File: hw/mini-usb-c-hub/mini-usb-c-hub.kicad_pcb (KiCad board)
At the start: 4 copper layers, 0 parts

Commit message: chore(hw): choose usb-c receptacle
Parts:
- added J1: USB_C_Receptacle_USB2.0_16P, local:USB_C_Receptacle_G-Switch_GT-USB-7010ASV_shortened, F.Cu at (172.3, 102.8)
- added R1: 5k1, Resistor_SMD:R_0805_2012Metric_Pad1.20x1.40mm_HandSolder, F.Cu at (154.1, 100.2)
- added R2: 5k1, Resistor_SMD:R_0805_2012Metric_Pad1.20x1.40mm_HandSolder, F.Cu at (154.1, 103.2)
- added U101: FE1.1s, Package_SO:SSOP-28_3.9x9.9mm_P0.635mm, F.Cu at (134.0, 106.8)
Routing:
- net unconnected-(J1-SHIELD-PadS1): track 0.00 -> 17.0 mm
- net +5V: track 0.00 -> 7.76 mm, vias 0 -> 2
- net GND: track 0.00 -> 5.63 mm, vias 0 -> 1
- net unconnected-(J1-D--PadB7): track 0.00 -> 2.98 mm
- net Net-(J1-CC1): track 0.00 -> 2.97 mm
- net unconnected-(J1-SBU2-PadB8): track 0.00 -> 2.97 mm
- added copper zone on B.Cu, net GND
- added copper zone on F.Cu, net GND
- added copper zone on In1.Cu, net GND
- added copper zone on In2.Cu, net GND
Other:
- board outline added: 80 x 40 mm

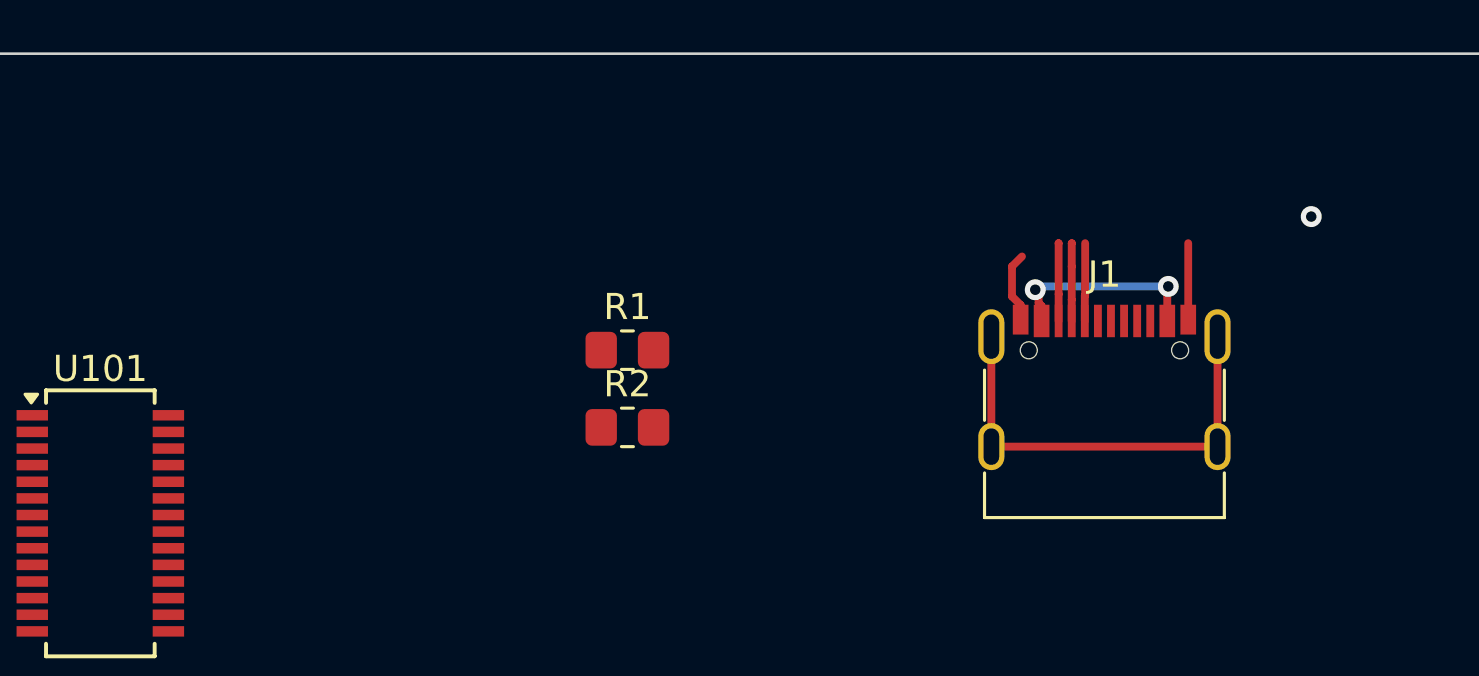
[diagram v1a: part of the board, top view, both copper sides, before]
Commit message: chore(hw): add data pins, move upstream connector
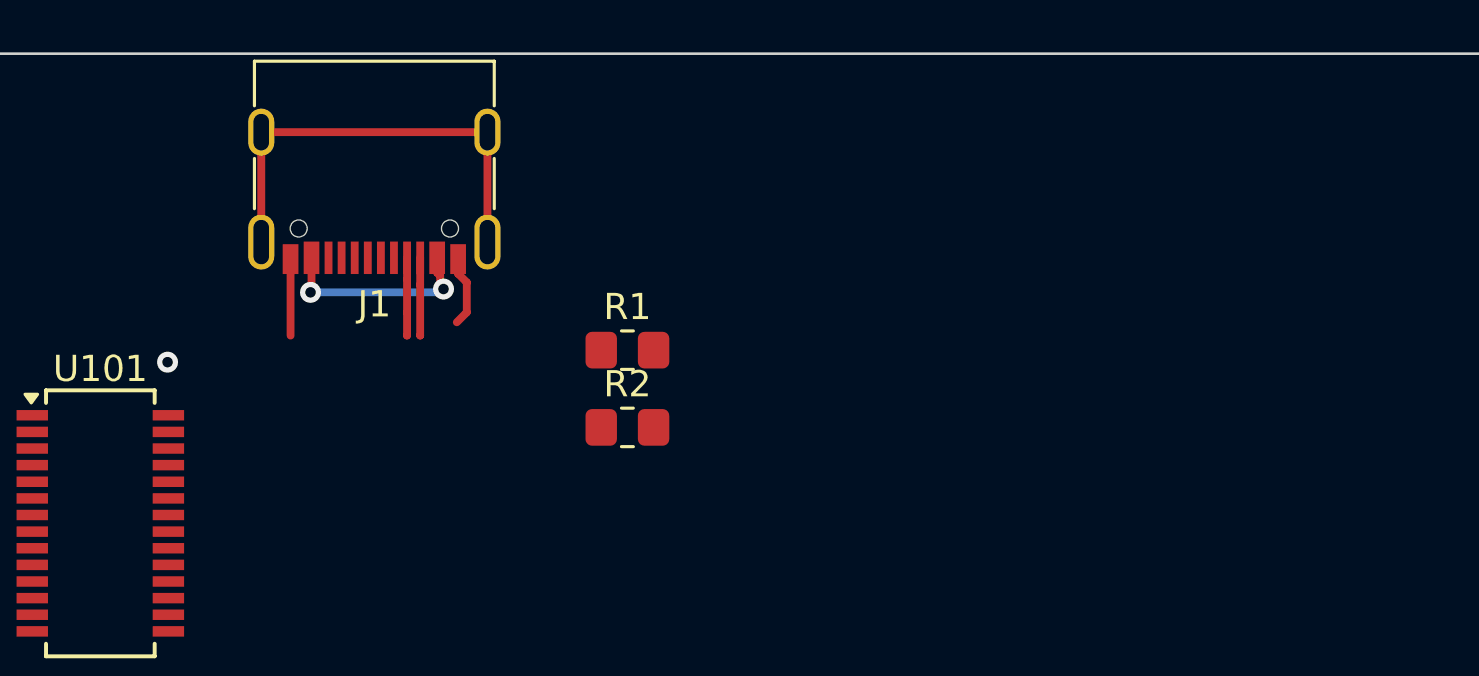
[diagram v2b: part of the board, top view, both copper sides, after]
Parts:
- moved J1 29.6 mm to (144.4, 93.0), turned to 180 degrees
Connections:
- J1 pad A6: unconnected-(J1-D+-PadA6) -> /Upstream Port/UD_P
- J1 pad A7: unconnected-(J1-D--PadA7) -> /Upstream Port/UD_N
- U101 pad 15: unconnected-(U101-DMU-Pad15) -> /Upstream Port/UD_N
- U101 pad 16: unconnected-(U101-DPU-Pad16) -> /Upstream Port/UD_P
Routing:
- net unconnected-(J1-D--PadB7): track 2.98 -> 0.00 mm

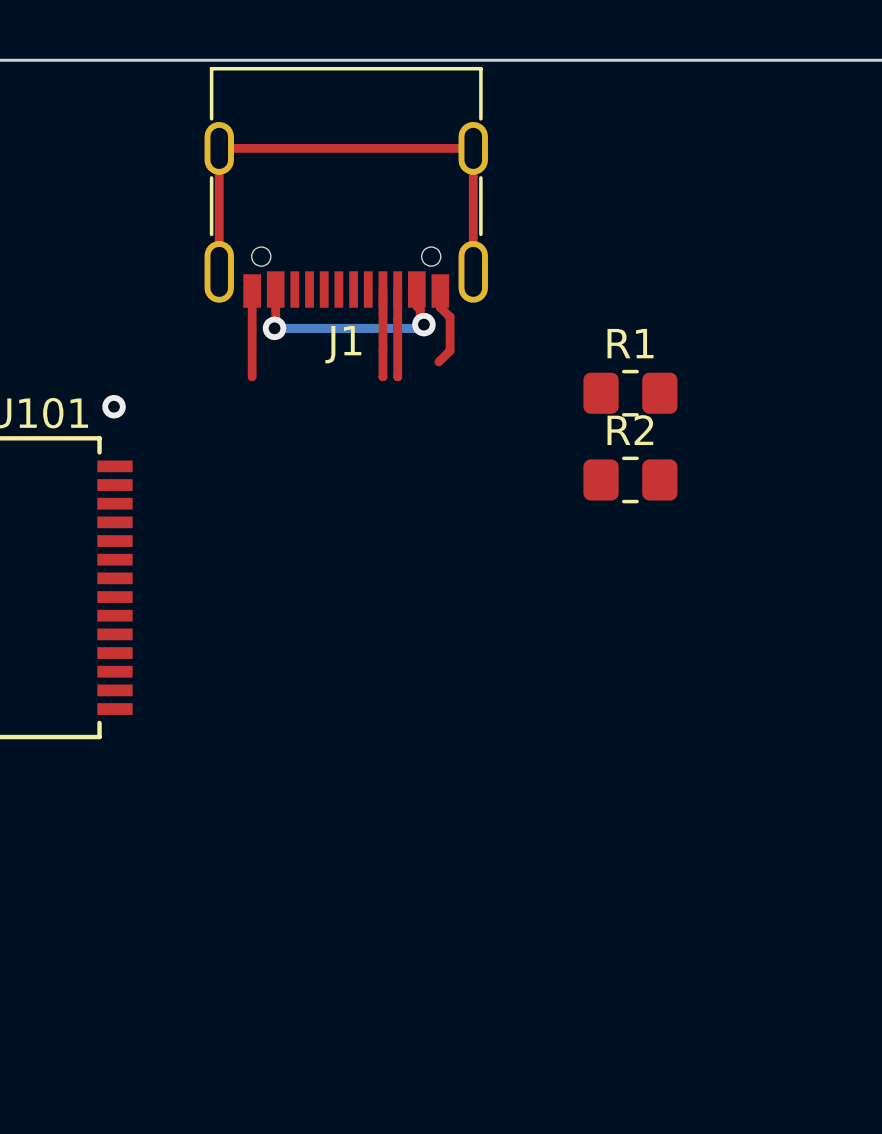
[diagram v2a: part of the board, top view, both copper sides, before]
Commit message: chore(hw): preliminary hub chip connections
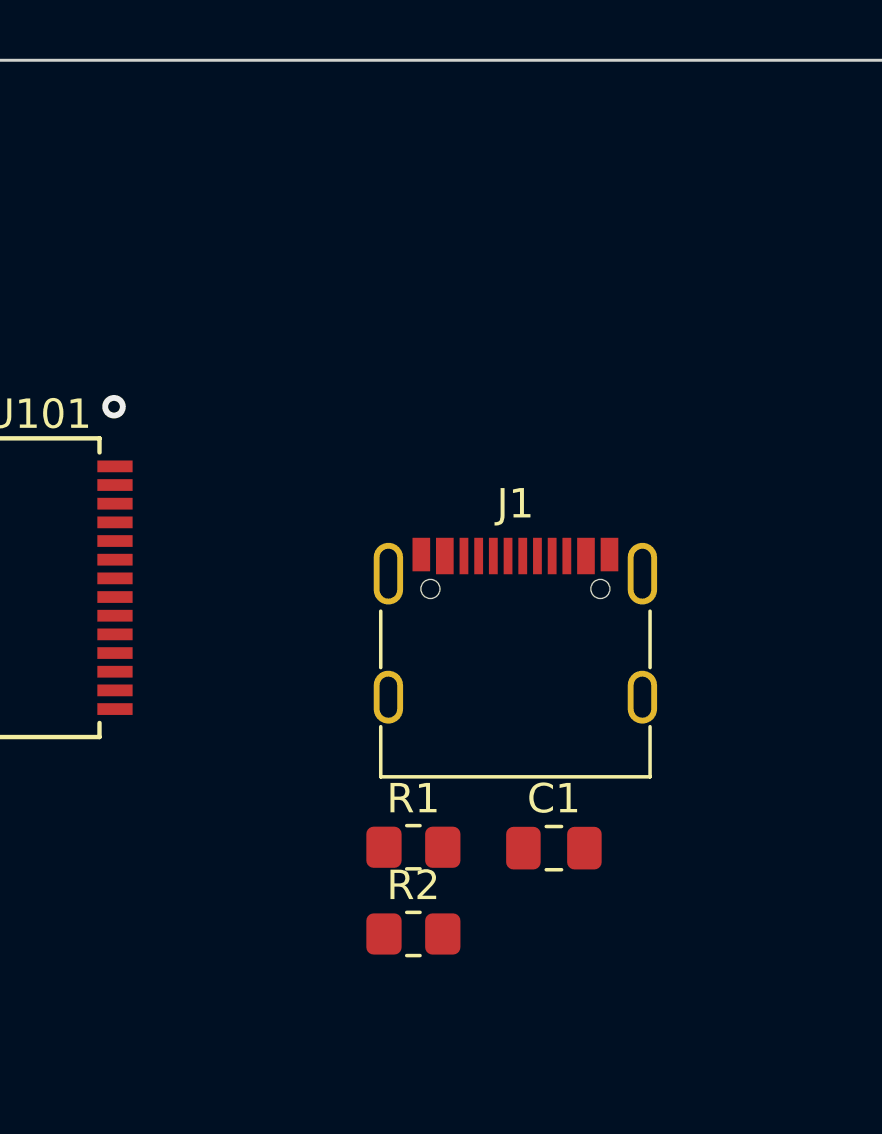
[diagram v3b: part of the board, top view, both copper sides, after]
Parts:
- added C1: C, Capacitor_SMD:C_0805_2012Metric_Pad1.18x1.45mm_HandSolder, F.Cu at (151.5, 115.7)
- moved J1 17.5 mm to (150.2, 109.5), turned to 0 degrees
- moved R1 17.1 mm to (146.7, 115.7)
- moved R2 17.1 mm to (146.7, 118.6)
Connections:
- net /Upstream Port/UD_N renamed /UD_N
- net /Upstream Port/UD_P renamed /UD_P
- J1 pad S1: unconnected-(J1-SHIELD-PadS1) -> Net-(J1-SHIELD)
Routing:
- net unconnected-(J1-SHIELD-PadS1): track 17.0 -> 0.00 mm
- net +5V: track 7.76 -> 0.00 mm, vias 2 -> 0
- net GND: track 5.63 -> 0.00 mm
- net Net-(J1-CC1): track 2.97 -> 0.00 mm
- net unconnected-(J1-SBU2-PadB8): track 2.97 -> 0.00 mm

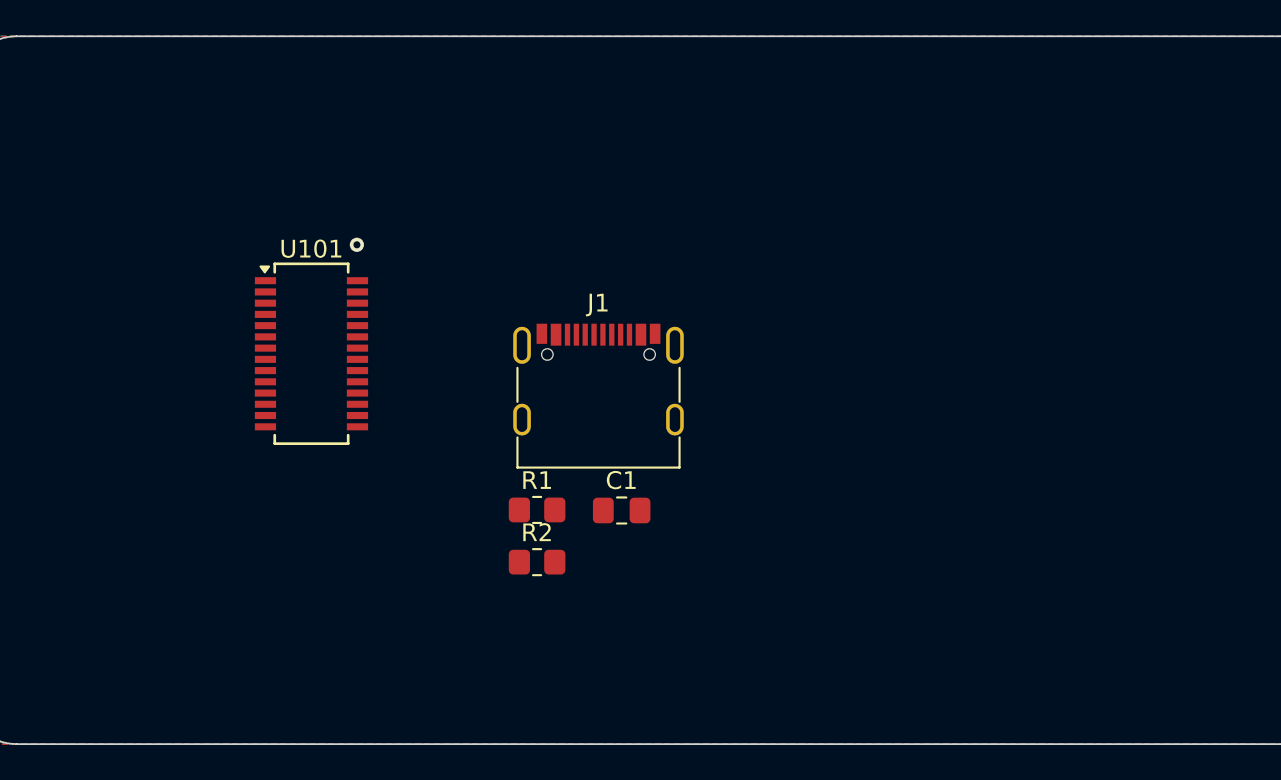
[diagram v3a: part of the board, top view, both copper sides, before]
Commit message: chore(hw): add downstream ports
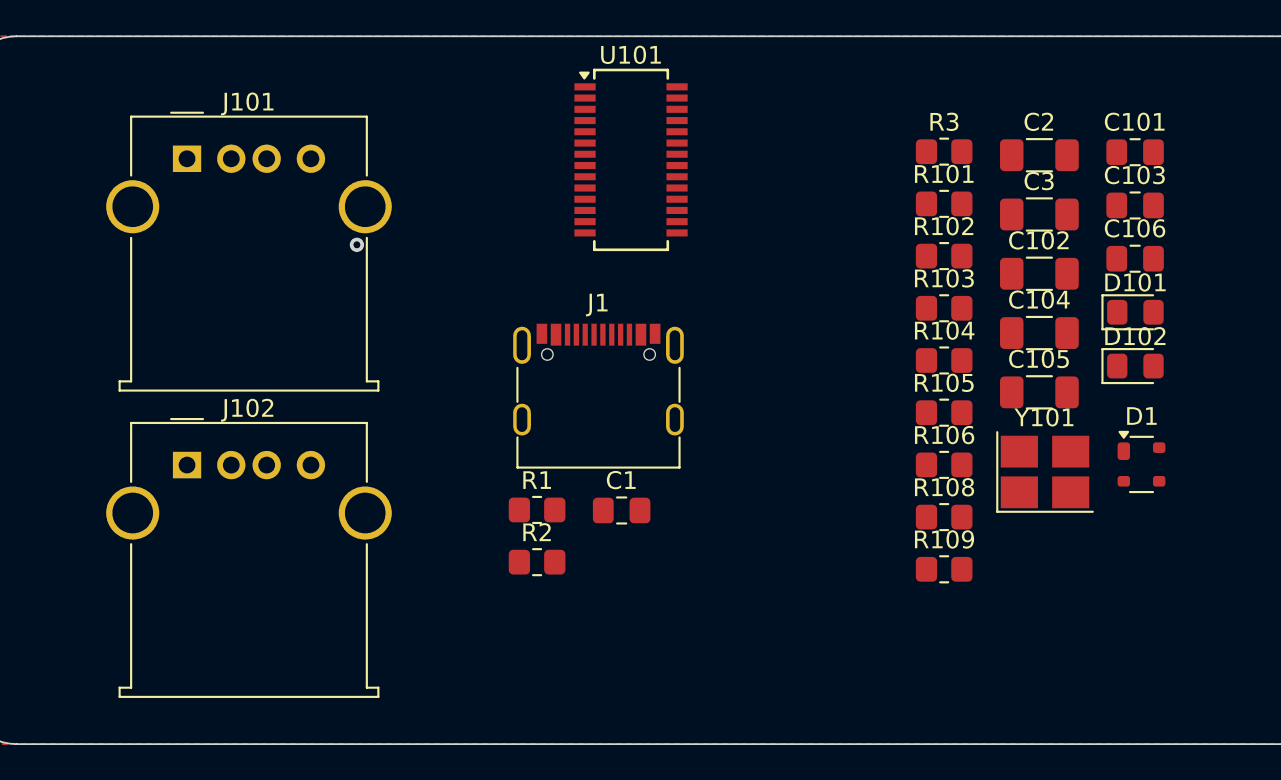
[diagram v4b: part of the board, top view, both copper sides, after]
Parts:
- added C101: 100n, Capacitor_SMD:C_0805_2012Metric_Pad1.18x1.45mm_HandSolder, F.Cu at (180.5, 95.5)
- added C102: 10u, Capacitor_SMD:C_1206_3216Metric_Pad1.33x1.80mm_HandSolder, F.Cu at (175.1, 102.3)
- added C103: 100n, Capacitor_SMD:C_0805_2012Metric_Pad1.18x1.45mm_HandSolder, F.Cu at (180.5, 98.5)
- added C104: 10u, Capacitor_SMD:C_1206_3216Metric_Pad1.33x1.80mm_HandSolder, F.Cu at (175.1, 105.7)
- added C105: 10u, Capacitor_SMD:C_1206_3216Metric_Pad1.33x1.80mm_HandSolder, F.Cu at (175.1, 109.0)
- added C106: 100n, Capacitor_SMD:C_0805_2012Metric_Pad1.18x1.45mm_HandSolder, F.Cu at (180.5, 101.5)
- added C2: 10p, Capacitor_SMD:C_1206_3216Metric_Pad1.33x1.80mm_HandSolder, F.Cu at (175.1, 95.6)
- added C3: 10p, Capacitor_SMD:C_1206_3216Metric_Pad1.33x1.80mm_HandSolder, F.Cu at (175.1, 99.0)
- added D1: PRTR5V0U2X, Package_TO_SOT_SMD:SOT-143, F.Cu at (180.9, 113.1)
- added D101: LED, LED_SMD:LED_0805_2012Metric_Pad1.15x1.40mm_HandSolder, F.Cu at (180.5, 104.5)
- added D102: LED, LED_SMD:LED_0805_2012Metric_Pad1.15x1.40mm_HandSolder, F.Cu at (180.5, 107.5)
- added J101: USB_A, Connector_USB:USB_A_Molex_67643_Horizontal, F.Cu at (126.9, 95.8)
- added J102: USB_A, Connector_USB:USB_A_Molex_67643_Horizontal, F.Cu at (126.9, 113.1)
- added R101: 100k, Resistor_SMD:R_0805_2012Metric_Pad1.20x1.40mm_HandSolder, F.Cu at (169.7, 98.4)
- added R102: 2k7 1%, Resistor_SMD:R_0805_2012Metric_Pad1.20x1.40mm_HandSolder, F.Cu at (169.7, 101.3)
- added R103: 100k, Resistor_SMD:R_0805_2012Metric_Pad1.20x1.40mm_HandSolder, F.Cu at (169.7, 104.3)
- added R104: 100k, Resistor_SMD:R_0805_2012Metric_Pad1.20x1.40mm_HandSolder, F.Cu at (169.7, 107.2)
- added R105: 100k, Resistor_SMD:R_0805_2012Metric_Pad1.20x1.40mm_HandSolder, F.Cu at (169.7, 110.2)
- added R106: 100k, Resistor_SMD:R_0805_2012Metric_Pad1.20x1.40mm_HandSolder, F.Cu at (169.7, 113.1)
- added R108: 300R, Resistor_SMD:R_0805_2012Metric_Pad1.20x1.40mm_HandSolder, F.Cu at (169.7, 116.1)
- added R109: 300R, Resistor_SMD:R_0805_2012Metric_Pad1.20x1.40mm_HandSolder, F.Cu at (169.7, 119.0)
- added R3: 0R, Resistor_SMD:R_0805_2012Metric_Pad1.20x1.40mm_HandSolder, F.Cu at (169.7, 95.4)
- added Y101: 12MHz, Crystal:Crystal_SMD_3225-4Pin_3.2x2.5mm_HandSoldering, F.Cu at (175.4, 113.5)
- C1: value C -> 10n 200V
- moved U101 21.1 mm to (152.0, 95.9)
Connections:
- J1 pad A6: /UD_P -> /UUSB+
- J1 pad A7: /UD_N -> /UUSB-
- J1 pad B6: unconnected-(J1-D+-PadB6) -> /UUSB+
- J1 pad B7: unconnected-(J1-D--PadB7) -> /UUSB-
- U101 pad 1: unconnected-(U101-VSS-Pad1) -> GND
- U101 pad 10: unconnected-(U101-DM1-Pad10) -> /D1USB-
- U101 pad 11: unconnected-(U101-DP1-Pad11) -> /D1USB+
- U101 pad 12: unconnected-(U101-VD18_O-Pad12) -> Net-(U101-VD18_O)
- U101 pad 13: unconnected-(U101-VD33-Pad13) -> Net-(U101-VD33)
- U101 pad 14: unconnected-(U101-REXT-Pad14) -> Net-(U101-REXT)
- U101 pad 15: /UD_N -> /UUSB-
- U101 pad 16: /UD_P -> /UUSB+
- U101 pad 17: unconnected-(U101-~{XRSTJ}-Pad17) -> Net-(U101-~{XRSTJ})
- U101 pad 18: unconnected-(U101-VBUSM-Pad18) -> Net-(U101-VBUSM)
- U101 pad 19: unconnected-(U101-BUSJ-Pad19) -> Net-(U101-BUSJ)
- U101 pad 2: unconnected-(U101-XOUT-Pad2) -> Net-(U101-XOUT)
- U101 pad 20: unconnected-(U101-VDD5-Pad20) -> +5V
- U101 pad 21: unconnected-(U101-VD33_O-Pad21) -> Net-(U101-VD33)
- U101 pad 22: unconnected-(U101-DRV-Pad22) -> Net-(U101-DRV)
- U101 pad 24: unconnected-(U101-LED2-Pad24) -> Net-(D102-K)
- U101 pad 26: unconnected-(U101-OVCJ-Pad26) -> +5V
- U101 pad 28: unconnected-(U101-VD18-Pad28) -> Net-(U101-VD18)
- U101 pad 3: unconnected-(U101-XIN-Pad3) -> Net-(U101-XIN)
- U101 pad 6: unconnected-(U101-DM3-Pad6) -> /D3USB-
- U101 pad 7: unconnected-(U101-DP3-Pad7) -> /D3USB+
- U101 pad 8: unconnected-(U101-DM2-Pad8) -> /D2USB-
- U101 pad 9: unconnected-(U101-DP2-Pad9) -> /D2USB+

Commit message: chore(hw): add some basic layout
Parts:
- removed the J101 at (126.9, 95.8)
- removed J102: USB_A, Connector_USB:USB_A_Molex_67643_Horizontal
- added D102: PRTR5V0U2X, Package_TO_SOT_SMD:SOT-143, F.Cu at (138.3, 93.5)
- added D301: PRTR5V0U2X, Package_TO_SOT_SMD:SOT-143, F.Cu at (133.1, 105.0)
- added D401: PRTR5V0U2X, Package_TO_SOT_SMD:SOT-143, F.Cu at (145.0, 140.7)
- added D501: PRTR5V0U2X, Package_TO_SOT_SMD:SOT-143, F.Cu at (124.8, 164.6)
- added J301: USB_A, Connector_USB:USB_A_Molex_67643_Horizontal, F.Cu at (120.8, 106.0)
- added J401: USB_A, Connector_USB:USB_A_Molex_67643_Horizontal, F.Cu at (138.8, 106.0)
- added J501: USB_A, Connector_USB:USB_A_Molex_67643_Horizontal, F.Cu at (156.8, 106.0)
- added P101: USB_C_Plug_USB3.0, local:USB_C_Plug_G-Switch_GT-USB-8016A, F.Cu at (130.3, 91.9)
- added R107: ?, Resistor_SMD:R_0805_2012Metric_Pad1.20x1.40mm_HandSolder, F.Cu at (203.1, 77.1)
- moved C1 66.8 mm to (218.3, 117.4)
- moved R1 66.8 mm to (213.5, 117.4)
- moved D101 57.9 mm to (125.2, 97.1), turned to -90 degrees
- moved C101 38.6 mm to (218.5, 89.0)
- moved C102 38.6 mm to (213.1, 95.8)
- moved C103 38.6 mm to (218.5, 92.0)
- moved C104 38.6 mm to (213.1, 99.2)
- moved C105 38.6 mm to (213.1, 102.5)
- moved C106 38.6 mm to (218.5, 95.0)
- moved C2 38.6 mm to (213.1, 89.1)
- moved C3 38.6 mm to (213.1, 92.5)
- moved D108 38.6 mm to (218.5, 98.0)
- moved D109 38.6 mm to (218.5, 101.0)
- moved R101 38.6 mm to (207.7, 91.9)
- moved R102 38.6 mm to (207.7, 94.8)
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- renumbered D1 to D101, D101 to D108, D102 to D109, J1 to J101
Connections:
- net Net-(U101-VD33) renamed +3.3V
- D101 pad 1: unconnected-(D1-GND-Pad1) -> GND
- D101 pad 2: unconnected-(D1-I/O1-Pad2) -> /UUSB-
- D101 pad 3: unconnected-(D1-I/O2-Pad3) -> /UUSB+
- D101 pad 4: unconnected-(D1-VCC-Pad4) -> +5V
- U101 pad 4: unconnected-(U101-DM4-Pad4) -> /D4USB-
- U101 pad 5: unconnected-(U101-DP4-Pad5) -> /D4USB+
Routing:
- net /D3USB+: track 0.00 -> 25.9 mm
- net /D3USB-: track 0.00 -> 25.1 mm
- net /D1USB+: track 0.00 -> 20.8 mm
- net /D1USB-: track 0.00 -> 19.5 mm
- net /D2USB+: track 0.00 -> 17.7 mm
- net /D2USB-: track 0.00 -> 17.0 mm
- net GND: vias 1 -> 0
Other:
- board size 80 x 40 mm -> 56 x 30 mm

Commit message: chore(hw): lay-out some differential pairs
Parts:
- added C201: 10u, Capacitor_SMD:C_1206_3216Metric_Pad1.33x1.80mm_HandSolder, F.Cu at (116.1, 113.3)
- added C301: 10u, Capacitor_SMD:C_1206_3216Metric_Pad1.33x1.80mm_HandSolder, F.Cu at (134.1, 113.3)
- added C401: 10u, Capacitor_SMD:C_1206_3216Metric_Pad1.33x1.80mm_HandSolder, F.Cu at (152.1, 113.3)
- moved C101 103.7 mm to (118.1, 90.4)
- moved R103 85.8 mm to (121.9, 90.4), turned to 180 degrees
- moved D401 73.4 mm to (162.4, 101.6), turned to 90 degrees
- moved D301 39.1 mm to (144.4, 101.6), turned to 90 degrees
- moved D201 7.55 mm to (126.4, 101.6), turned to 90 degrees
- moved D102 6.67 mm to (132.7, 97.2), turned to 90 degrees
- moved U101 3.47 mm to (153.8, 96.8), turned to 90 degrees
- moved D101 0.19 mm to (125.0, 97.2)
- renumbered C1 to C101, C104 to C102, C102 to C104, C101 to C105, C2 to C106, C3 to C107, C105 to C108, C106 to C109, D109 to D103, D108 to D104, D301 to D201, D401 to D301, D501 to D401, J301 to J201, J401 to J301, J501 to J401, R1 to R101, R2 to R102, R101 to R103, R3 to R104, R106 to R105, R103 to R106, R104 to R108, R105 to R109, R109 to R110, R102 to R111, R108 to R112
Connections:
- D101 pad 2: /UUSB- -> /UUSB+
- D101 pad 3: /UUSB+ -> /UUSB-
- D102 pad 2: /D1USB- -> /D1USB+
- D102 pad 3: /D1USB+ -> /D1USB-
- D201 pad 2: /D4USB- -> /D4USB+
- D201 pad 3: /D4USB+ -> /D4USB-
- D301 pad 2: /D3USB- -> /D3USB+
- D301 pad 3: /D3USB+ -> /D3USB-
- D401 pad 2: /D2USB- -> /D2USB+
- D401 pad 3: /D2USB+ -> /D2USB-
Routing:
- net +5V: track 0.00 -> 63.9 mm, vias 0 -> 5
- net /UUSB-: track 0.00 -> 40.8 mm
- net /UUSB+: track 0.00 -> 39.9 mm
- net /D4USB-: track 0.00 -> 28.9 mm
- net /D4USB+: track 0.00 -> 28.2 mm
- net Net-(J101-SHIELD): track 0.00 -> 23.3 mm
- net /D2USB+: track 17.7 -> 0.00 mm
- net /D2USB-: track 17.0 -> 0.00 mm
- net /D1USB+: track 20.8 -> 6.66 mm
- net /D1USB-: track 19.5 -> 5.94 mm
- net /D3USB+: track 25.9 -> 17.8 mm
- net /D3USB-: track 25.1 -> 17.8 mm
- net GND: track 0.00 -> 3.11 mm, vias 0 -> 8
- added copper zone on B.Cu, net +5V
